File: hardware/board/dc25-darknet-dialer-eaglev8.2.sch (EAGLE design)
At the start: 96 parts, among them J1 MF-CON-MICROUSB-RIGHT, SW1 RESET, U1 BU33SD5WG-TR, U2 MCP73831T-5ACI/OT, U3 SOP22FLAT, Y1 CSTCE8M00G52-R0

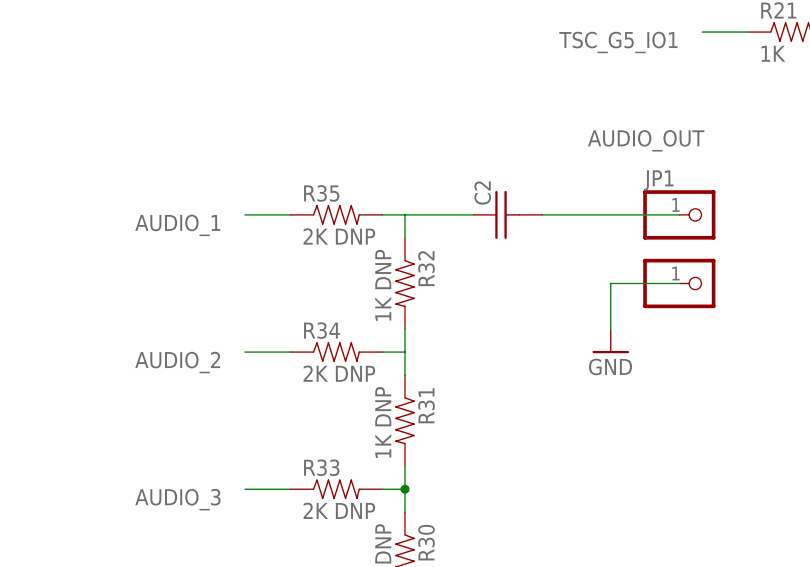
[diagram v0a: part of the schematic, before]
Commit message: updated schematic to populate audio
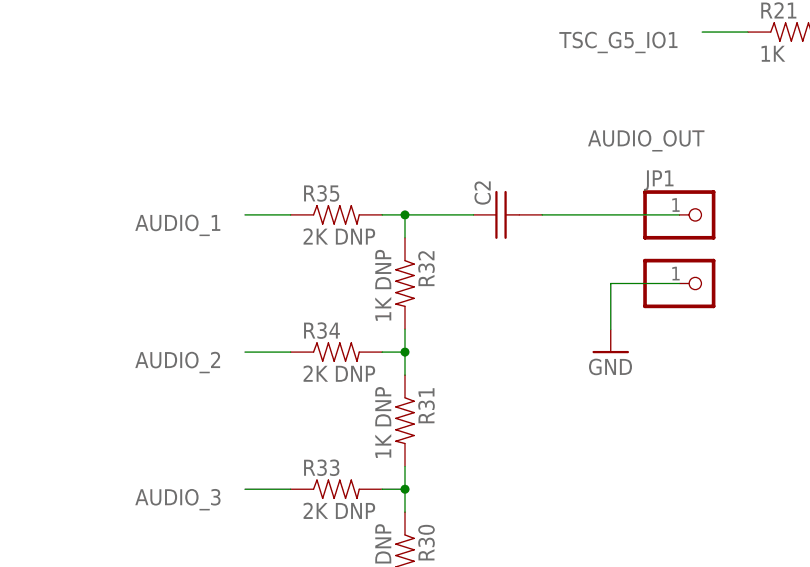
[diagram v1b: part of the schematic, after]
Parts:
- C2: value 10uF DNP -> GRM188C80G106ME47D
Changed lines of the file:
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@@
 <part name="R32" library="darknet_parts_library" deviceset="RESISTOR" device="0603-RES" value="1K DNP"/>
 <part name="R35" library="darknet_parts_library" deviceset="RESISTOR" device="0603-RES" value="2K DNP"/>
-<part name="C2" library="darknet_parts_library" deviceset="C-US" device="C0603" value="10uF DNP"/>
+<part name="C2" library="darknet_parts_library" deviceset="C-US" device="C0603" value="GRM188C80G106ME47D"/>
 <part name="R30" library="darknet_parts_library" deviceset="RESISTOR" device="0603-RES" value="2K DNP"/>
 <part name="GND17" library="SYNShop" deviceset="GND" device=""/>
@@
 <wire x1="264.16" y1="38.1" x2="271.78" y2="38.1" width="0.1524" layer="91"/>
 <wire x1="264.16" y1="35.56" x2="264.16" y2="38.1" width="0.1524" layer="91"/>
+<junction x="264.16" y="38.1"/>
 </segment>
 </net>
@@
 <wire x1="264.16" y1="22.86" x2="264.16" y2="20.32" width="0.1524" layer="91"/>
 <wire x1="261.62" y1="22.86" x2="264.16" y2="22.86" width="0.1524" layer="91"/>
-</segment>
-</net>
+<junction x="264.16" y="22.86"/>
+</segment>
+</net>

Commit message: Helps if one saves
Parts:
- R30, R33, R34, R35: value 2K DNP -> 2K
- R31, R32: value 1K DNP -> 1K
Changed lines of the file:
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@@
 <part name="J1" library="MF_Connectors" deviceset="USB" device="_MICRO_RIGHT" value="MF-CON-MICROUSB-RIGHT"/>
 <part name="U$11" library="darknet_parts_library" deviceset="SWITCH_SPDT" device=""/>
-<part name="R33" library="darknet_parts_library" deviceset="RESISTOR" device="0603-RES" value="2K DNP"/>
-<part name="R31" library="darknet_parts_library" deviceset="RESISTOR" device="0603-RES" value="1K DNP"/>
-<part name="R34" library="darknet_parts_library" deviceset="RESISTOR" device="0603-RES" value="2K DNP"/>
-<part name="R32" library="darknet_parts_library" deviceset="RESISTOR" device="0603-RES" value="1K DNP"/>
-<part name="R35" library="darknet_parts_library" deviceset="RESISTOR" device="0603-RES" value="2K DNP"/>
+<part name="R33" library="darknet_parts_library" deviceset="RESISTOR" device="0603-RES" value="2K"/>
+<part name="R31" library="darknet_parts_library" deviceset="RESISTOR" device="0603-RES" value="1K"/>
+<part name="R34" library="darknet_parts_library" deviceset="RESISTOR" device="0603-RES" value="2K"/>
+<part name="R32" library="darknet_parts_library" deviceset="RESISTOR" device="0603-RES" value="1K"/>
+<part name="R35" library="darknet_parts_library" deviceset="RESISTOR" device="0603-RES" value="2K"/>
 <part name="C2" library="darknet_parts_library" deviceset="C-US" device="C0603" value="GRM188C80G106ME47D"/>
-<part name="R30" library="darknet_parts_library" deviceset="RESISTOR" device="0603-RES" value="2K DNP"/>
+<part name="R30" library="darknet_parts_library" deviceset="RESISTOR" device="0603-RES" value="2K"/>
 <part name="GND17" library="SYNShop" deviceset="GND" device=""/>
 <part name="GND18" library="SYNShop" deviceset="GND" device=""/>

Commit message: Updated library for new logo
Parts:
- U$1: value DN_LOGO -> DN_LOGODC25; device SYNShop:DN_LOGO -> SYNShop:DN_LOGODC25
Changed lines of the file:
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@@
 </classes>
 <parts>
-<part name="U$1" library="SYNShop" deviceset="DN_LOGO" device=""/>
+<part name="U$1" library="SYNShop" deviceset="DN_LOGO" device="DC25"/>
 <part name="TOUCH1" library="darknet_parts_library" deviceset="CAP_TOUCH" device="1"/>
 <part name="TOUCH2" library="darknet_parts_library" deviceset="CAP_TOUCH" device="2" value="CAP_TOUCH2"/>
